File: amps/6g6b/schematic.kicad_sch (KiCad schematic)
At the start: 91 parts, among them T1 125P7A, T3 125A13A

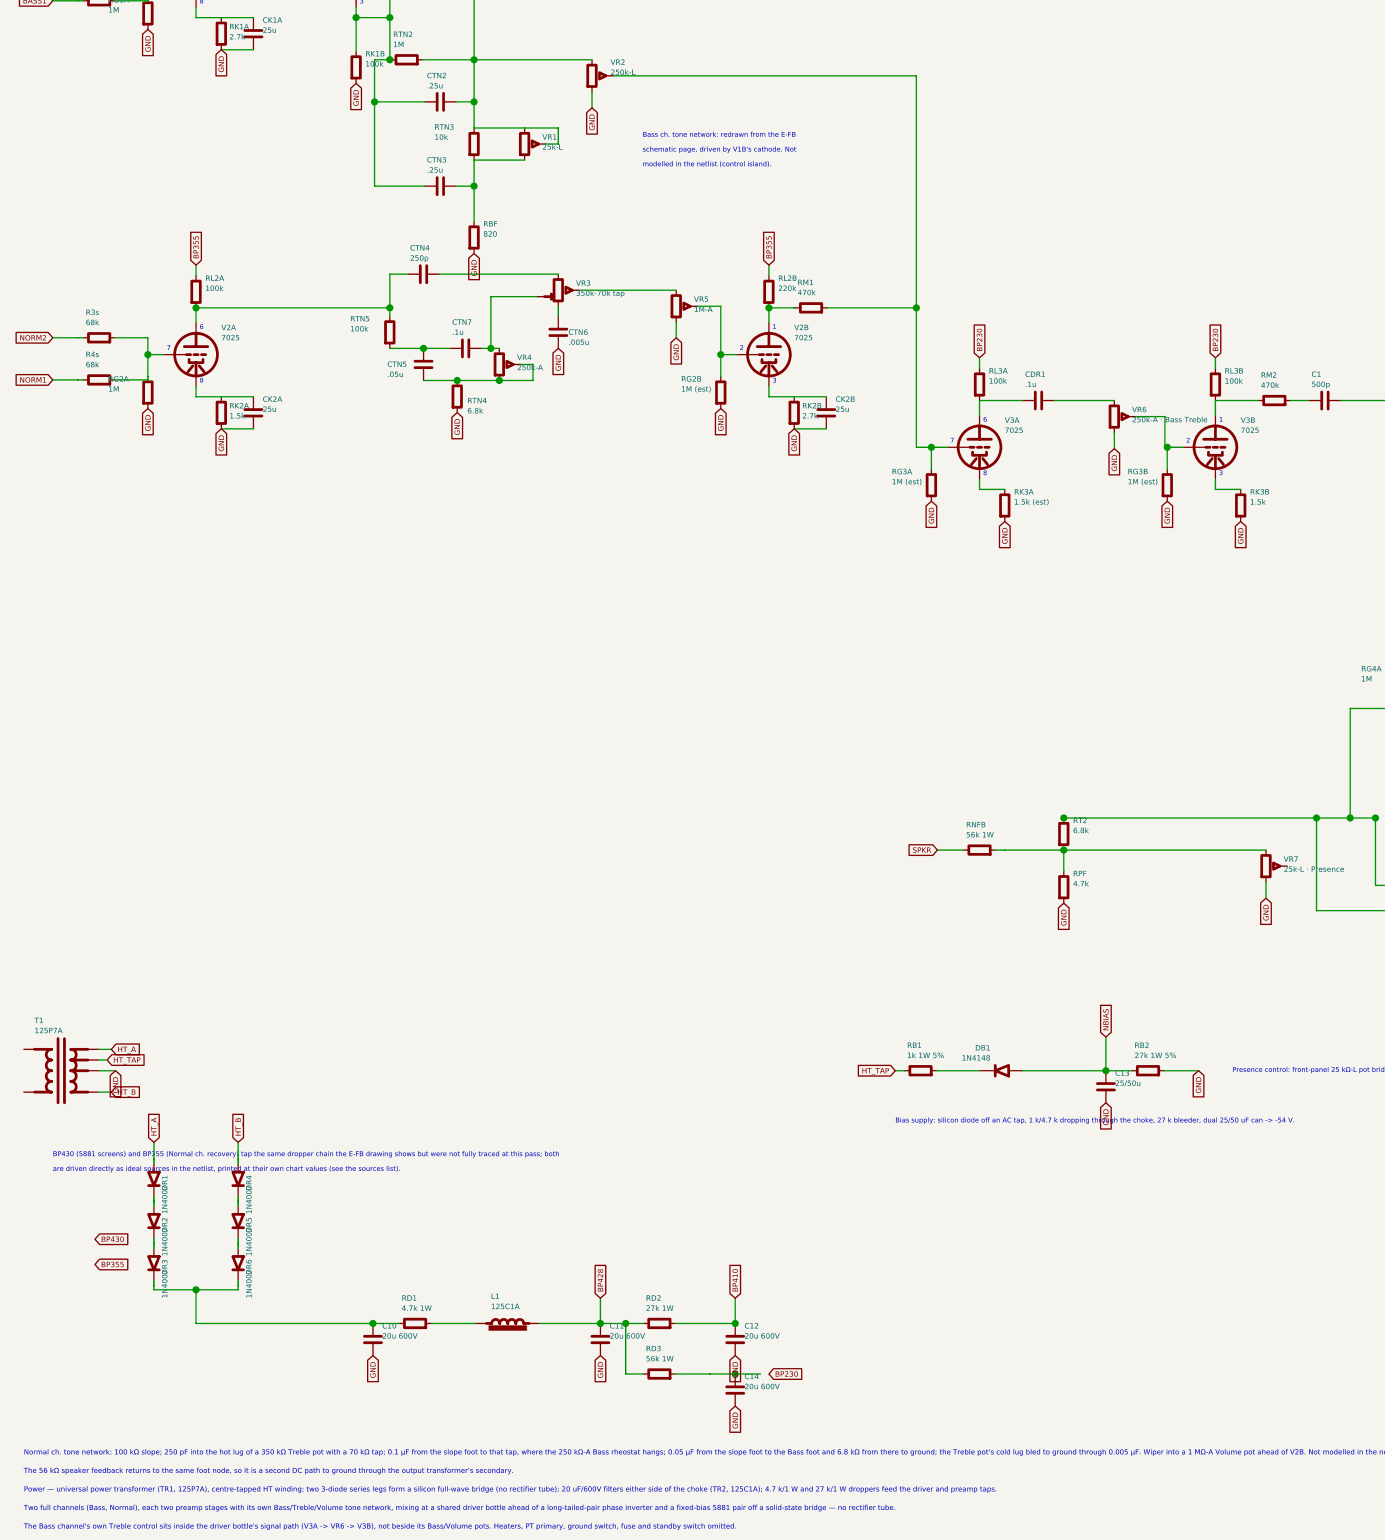
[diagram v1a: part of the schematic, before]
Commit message: Fix: 6G6-B mixed the Normal channel into V3A's grid; E-FB lands its 470K after V3B, at the node that feeds the phase inverter
- The E-FB schematic takes the Normal channel's V2B plate (+190 V) through
  a 470K up the right-hand vertical to the node where the Bass channel's
  V3B plate lands through its own 470K. That node feeds the .0005 into the
  phase-inverter grid. V3A's grid gets only the Bass Volume's wiper. V3 is
  therefore the Bass channel's second and third gain stages, not a driver
  both channels share. The sheet had RM1 landing on the MIXG bus at V3A's
  grid, and the netlist header, BOM roles, chart notes, meta and notes all
  called V3 a shared driver.
- The netlist now models the node: RM2 P3B->MIX, RM1 P2B->MIX, C1 MIX->G4A.
  Neither plate has a capacitor ahead of its 470K, so the pair is a 940k DC
  path between the two plates carrying about 40 uA. P2B moves
  202.8 -> 196.4 V (the chart prints 190; 6.7% -> 3.3%), P3B moves
  148.7 -> 151.9 V, and every node stays in tolerance. RM2's sch_map
  series_bridge is retired now that RM2 is a netlist part.
- Board, from the E-FB layout page: RM2 runs from the "A" turret (V3B's
  plate, the eyelet carrying the 100K || .002) to a mid-board eyelet. That
  eyelet also takes the diagonal 470K from V2B's plate (the eyelet with the
  220K off +355 V) and the .0005 to the phase inverter. The board had RM2.b
  wired to nothing, C1 hanging on RM2.a with the V3B plate, and RM1 on the
  MIXG lane. RM2.b -> C1.a and RM1.b -> RM2.b now; the MIXG lane runs V3A's
  grid straight to the Bass Volume's wiper.
- verify_schematic_nets, verify_layout_nets and verify_sheet_vs_board are
  clean on RM1, RM2 and C1. RM2 is off the MISPLACED list. CTN2, CTN3 and
  the sheet-only C14/RD3 rows predate this change.

Co-Authored-By: Claude Opus 5 (1M context) <noreply@anthropic.com>
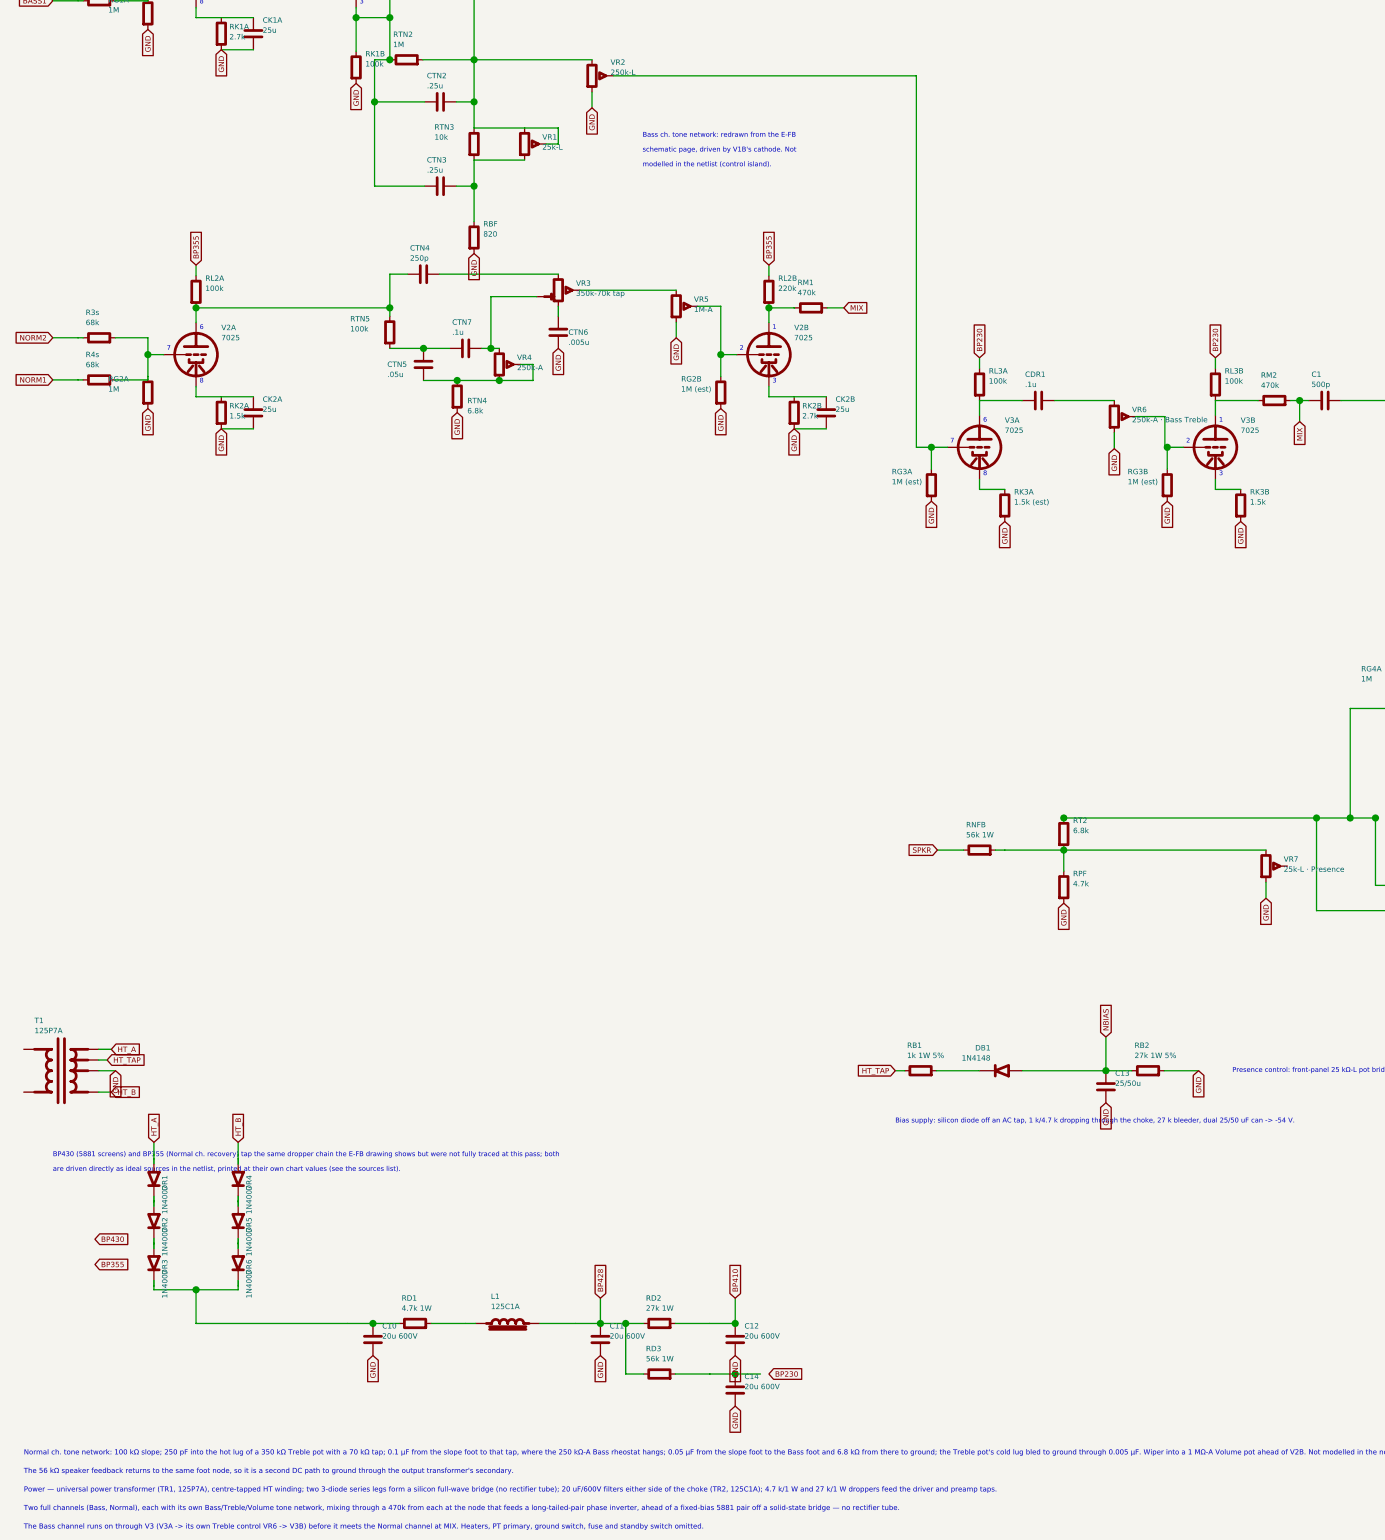
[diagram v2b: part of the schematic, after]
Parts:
- removed CK2A, CK2B: 25u, symbol cx:C
- removed RB1: 1k 1W 5%, symbol cx:R
- removed RD1: 4.7k 1W, symbol cx:R
- removed RD2: 27k 1W, symbol cx:R
- removed RD3: 56k 1W, symbol cx:R
- removed V5, V6: 5881, symbol cx:PENTODE
- removed VR4: 250k-A, symbol cx:POT
- added C11, C12, C14: 20u 600V, symbol cx:C
- added C13: 25/50u, symbol cx:C
- added CTN5: .05u, symbol cx:C
- added RGL5, RGL6: 220k, symbol cx:R
- added RK2A: 1.5k, symbol cx:R
- added RK2B: 2.7k, symbol cx:R
- CK2A: renamed from RK2A; value 1.5k -> 25u; symbol cx:R -> cx:C
- CK2B: renamed from RK2B; value 2.7k -> 25u; symbol cx:R -> cx:C
- DB1: renamed from C13; value 25/50u -> 1N4148; symbol cx:C -> cx:DIODE_SS
- L1: renamed from C11; value 20u 600V -> 125C1A; symbol cx:C -> cx:CHOKE
- RB1: renamed from DB1; value 1N4148 -> 1k 1W 5%; symbol cx:DIODE_SS -> cx:R
- RD1: renamed from L1; value 125C1A -> 4.7k 1W; symbol cx:CHOKE -> cx:R
- RD2: renamed from C12; value 20u 600V -> 27k 1W; symbol cx:C -> cx:R
- RD3: renamed from C14; value 20u 600V -> 56k 1W; symbol cx:C -> cx:R
- V5: renamed from RGL5; value 220k -> 5881; symbol cx:R -> cx:PENTODE
- V6: renamed from RGL6; value 220k -> 5881; symbol cx:R -> cx:PENTODE
- VR4: renamed from CTN5; value .05u -> 250k-A; symbol cx:C -> cx:POT
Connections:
- net BP410: now also RD2.2, C12.1; no longer RD2.1
- net BP428: now also L1.2, RD2.1, RD3.1, C11.1; no longer L1.1, RD1.2
- net GND: now also V5.4 (K), V6.4 (K), C11.2, C12.2, C13.2, C14.2, RK2A.2, RK2B.2; no longer DB1.2, L1.2, RD2.2, RD3.2
- net HT_TAP: now also RB1.1
- net NBIAS: now also C13.1, RGL5.2, RGL6.2; no longer RB1.1 (A), V5.2, V6.2
- net at RTN4.1, VR4.2 (W): now also VR4.3, CTN5.2
- net at C2.2: now also V5.2 (G1), RGL5.1; no longer V5.1
- net at CTN7.1, RTN5.2: now also CTN5.1; no longer VR4.1
- net MIX: now reaches C1.1, RM2.2
- net MIX: now also RM1.2
- net at CK2B.1, V2B.3 (K): now also RK2B.1
- net at RG3A.1, V3A.2 (G), VR2.2 (W): no longer RM1.2
- net at RS5.1: now also V5.3 (G2)
- net at CK2A.1, V2A.3 (K): now also RK2A.1
- net at C10.1, DR3.2 (K), DR6.2 (K): now also RD1.1
- net at CTN7.2, VR3.4 (T): now also VR4.1
- net at T3.3 (PRI_B): now also V6.1 (P)
- net at C3.2: now also V6.2 (G1), RGL6.1; no longer V6.1
- net at RS6.1: now also V6.3 (G2)
- net at T3.1 (PRI_A): now also V5.1 (P)
- net at RB1.2: now also DB1.2 (K)
- new net: L1.1, RD1.2
- new net: C14.1, RD3.2
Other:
- note added: "The Bass channel runs on through V3 (V3A -> its own Treble control VR6 -> V3B) before it meets the Normal channel at MIX. Heaters, PT primary, ground switch, fuse and standby switch omitted."
- note added: "Two full channels (Bass, Normal), each with its own Bass/Treble/Volume tone network, mixing through a 470k from each at the node that feeds a long-tailed-pair phase inverter, ahead of a fixed-bias 5881 pair off a solid-state bridge — no rectifier tube."
- note removed: "The Bass channel's own Treble control sits inside the driver bottle's signal path (V3A -> VR6 -> V3B), not beside its Bass/Volume pots. Heaters, PT primary, ground switch, fuse and standby switch omitted."
- note removed: "Two full channels (Bass, Normal), each two preamp stages with its own Bass/Treble/Volume tone network, mixing at a shared driver bottle ahead of a long-tailed-pair phase inverter and a fixed-bias 5881 pair off a solid-state bridge — no rectifier tube."
- moved on the sheet: DB1
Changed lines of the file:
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@@
   (wire (pts (xy 152.67 63.8152) (xy 224.59 63.8152))
     (stroke (width 0) (type default)))
-  (wire (pts (xy 224.59 63.8152) (xy 224.59 118.905))
-    (stroke (width 0) (type default)))
-  (wire (pts (xy 224.59 118.905) (xy 224.59 152.005))
+  (wire (pts (xy 224.59 63.8152) (xy 224.59 152.005))
     (stroke (width 0) (type default)))
   (text "Bass ch. tone network: redrawn from the E-FB" (at 159.59 78.0052 0)
@@
   (wire (pts (xy 195.59 118.905) (xy 195.78 118.905))
     (stroke (width 0) (type default)))
-  (wire (pts (xy 203.4 118.905) (xy 224.59 118.905))
-    (stroke (width 0) (type default)))
-  (junction (at 224.59 118.905) (diameter 1.7) (color 0 0 0 0))
+  (wire (pts (xy 203.4 118.905) (xy 207.4 118.905))
+    (stroke (width 0) (type default)))
+  (global_label "MIX" (shape input) (at 207.4 118.905 0)
+    (effects (font (size 1.27 1.27)) (justify left)))
   (symbol (lib_id "cx:TRIODE") (at 239.59 152.005 0) (unit 1)
     (in_bom yes) (on_board yes)
@@
     (property "Reference" "C1" (at 318.39 134.705 270) (effects (font (size 1.27 1.27)) (justify left)))
     (property "Value" "500p" (at 318.39 137.105 270) (effects (font (size 1.27 1.27)) (justify left))))
-  (wire (pts (xy 313.4 140.905) (xy 317.78 140.905))
-    (stroke (width 0) (type default)))
+  (wire (pts (xy 313.4 140.905) (xy 315.59 140.905))
+    (stroke (width 0) (type default)))
+  (wire (pts (xy 315.59 140.905) (xy 317.78 140.905))
+    (stroke (width 0) (type default)))
+  (junction (at 315.59 140.905) (diameter 1.7) (color 0 0 0 0))
+  (wire (pts (xy 315.59 140.905) (xy 315.59 145.905))
+    (stroke (width 0) (type default)))
+  (global_label "MIX" (shape input) (at 315.59 145.905 270)
+    (effects (font (size 1.27 1.27)) (justify right)))
   (wire (pts (xy 325.4 140.905) (xy 339.59 140.905))
     (stroke (width 0) (type default)))
@@
   (text "Power — universal power transformer (TR1, 125P7A), centre-tapped HT winding; two 3-diode series legs form a silicon full-wave bridge (no rectifier tube); 20 uF/600V filters either side of the choke (TR2, 125C1A); 4.7 k/1 W and 27 k/1 W droppers feed the driver and preamp taps." (at 12.7 399.583 0)
     (effects (font (size 1.2 1.2)) (justify left)))
-  (text "Two full channels (Bass, Normal), each two preamp stages with its own Bass/Treble/Volume tone network, mixing at a shared driver bottle ahead of a long-tailed-pair phase inverter and a fixed-bias 5881 pair off a solid-state bridge — no rectifier tube." (at 12.7 403.983 0)
+  (text "Two full channels (Bass, Normal), each with its own Bass/Treble/Volume tone network, mixing through a 470k from each at the node that feeds a long-tailed-pair phase inverter, ahead of a fixed-bias 5881 pair off a solid-state bridge — no rectifier tube." (at 12.7 403.983 0)
     (effects (font (size 1.2 1.2)) (justify left)))
-  (text "The Bass channel's own Treble control sits inside the driver bottle's signal path (V3A -> VR6 -> V3B), not beside its Bass/Volume pots. Heaters, PT primary, ground switch, fuse and standby switch omitted." (at 12.7 408.383 0)
+  (text "The Bass channel runs on through V3 (V3A -> its own Treble control VR6 -> V3B) before it meets the Normal channel at MIX. Heaters, PT primary, ground switch, fuse and standby switch omitted." (at 12.7 408.383 0)
     (effects (font (size 1.2 1.2)) (justify left)))
   (sheet_instances (path "/" (page "1")))
